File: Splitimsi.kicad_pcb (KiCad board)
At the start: 2 copper layers, 117.1 x 99.1 mm, 34 parts, among them SW1 MX_RGB, SW10 MX_RGB, SW11 MX_RGB, SW12 MX_RGB, SW13 MX_RGB, SW14 MX_RGB, SW15 MX_RGB, SW16 RotaryEncoder_Switch, SW17 MX_RGB, SW18 MX_RGB, SW19 MX_RGB, SW2 MX_RGB, SW20 MX_RGB, SW21 MX_RGB, SW22 MX_RGB, SW23 MX_RGB, SW24 MX_RGB, SW25 MX_RGB, SW26 MX_RGB, SW27 MX_RGB, SW28 MX_RGB, SW3 MX_RGB, SW4 MX_RGB, SW5 MX_RGB, SW6 MX_RGB, SW7 MX_RGB, SW8 MX_RGB, SW9 MX_RGB, U1 ProMicro, U2 TRRS

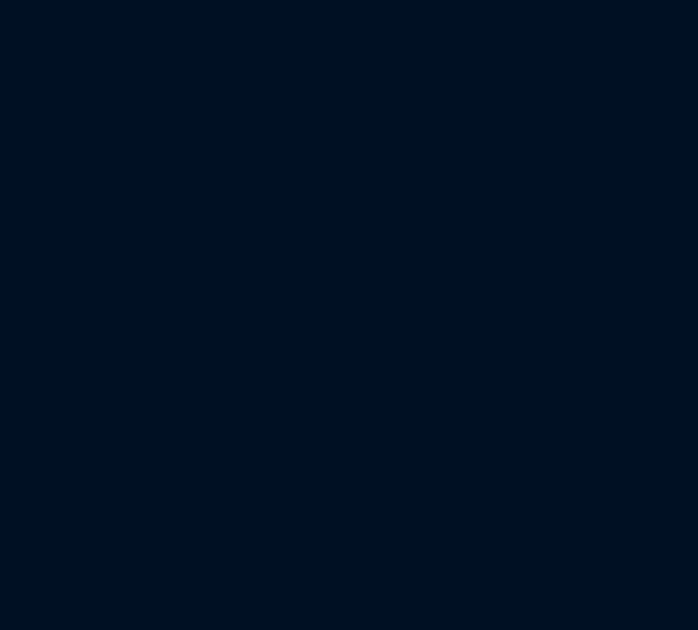
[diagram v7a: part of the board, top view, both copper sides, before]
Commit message: mounting holes added
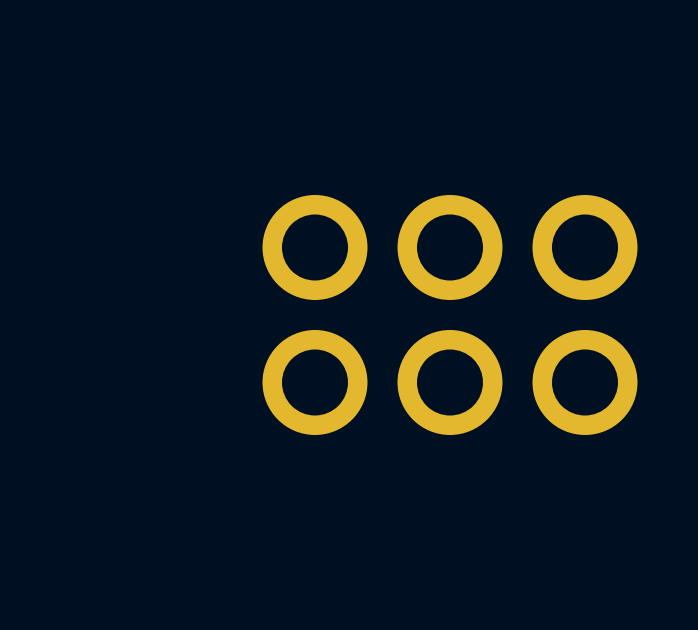
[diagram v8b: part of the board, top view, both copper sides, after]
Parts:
- added H1: Hole, aio3-misc:Generic-Mounthole, F.Cu at (167.0, 47.8)
- added H2: Hole, aio3-misc:Generic-Mounthole, F.Cu at (162.5, 47.8)
- added H3: Hole, aio3-misc:Generic-Mounthole, F.Cu at (158.0, 52.3)
- added H4: Hole, aio3-misc:Generic-Mounthole, F.Cu at (167.0, 52.3)
- added H5: Hole, aio3-misc:Generic-Mounthole, F.Cu at (158.0, 47.8)
- added H6: Hole, aio3-misc:Generic-Mounthole, F.Cu at (162.5, 52.3)
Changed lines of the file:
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@@
     )
+  )
+  (footprint "aio3-misc:Generic-Mounthole" (layer "F.Cu")
+    (at 157.992847 47.811959)
+    (property "Sheetfile" "Splitimsi.kicad_sch")
+    (property "Sheetname" "")
+    (attr exclude_from_pos_files)
+    (fp_text reference "H5" (at 0 2) (layer "Dwgs.User")
+      (effects (font (size 1 1) (thickness 0.15)))
+    )
+    (fp_text value "Hole" (at 0 -2) (layer "Dwgs.User")
+      (effects (font (size 1 1) (thickness 0.15)))
+    )
+    (pad "1" thru_hole circle locked (at 0 0) (size 3.5 3.5) (drill 2.2) (layers *.Cu *.Mask))
+  )
+  (footprint "aio3-misc:Generic-Mounthole" (layer "F.Cu")
+    (at 157.992847 52.311959)
+    (property "Sheetfile" "Splitimsi.kicad_sch")
+    (property "Sheetname" "")
+    (attr exclude_from_pos_files)
+    (fp_text reference "H3" (at 0 2) (layer "Dwgs.User")
+      (effects (font (size 1 1) (thickness 0.15)))
+    )
+    (fp_text value "Hole" (at 0 -2) (layer "Dwgs.User")
+      (effects (font (size 1 1) (thickness 0.15)))
+    )
+    (pad "1" thru_hole circle locked (at 0 0) (size 3.5 3.5) (drill 2.2) (layers *.Cu *.Mask))
+  )
+  (footprint "aio3-misc:Generic-Mounthole" (layer "F.Cu")
+    (at 162.492847 52.311959)
+    (property "Sheetfile" "Splitimsi.kicad_sch")
+    (property "Sheetname" "")
+    (attr exclude_from_pos_files)
+    (fp_text reference "H6" (at 0 2) (layer "Dwgs.User")
+      (effects (font (size 1 1) (thickness 0.15)))
+    )
+    (fp_text value "Hole" (at 0 -2) (layer "Dwgs.User")
+      (effects (font (size 1 1) (thickness 0.15)))
+    )
+    (pad "1" thru_hole circle locked (at 0 0) (size 3.5 3.5) (drill 2.2) (layers *.Cu *.Mask))
+  )
+  (footprint "aio3-misc:Generic-Mounthole" (layer "F.Cu")
+    (at 166.992847 47.811959)
+    (property "Sheetfile" "Splitimsi.kicad_sch")
+    (property "Sheetname" "")
+    (attr exclude_from_pos_files)
+    (fp_text reference "H1" (at 0 2) (layer "Dwgs.User")
+      (effects (font (size 1 1) (thickness 0.15)))
+    )
+    (fp_text value "Hole" (at 0 -2) (layer "Dwgs.User")
+      (effects (font (size 1 1) (thickness 0.15)))
+    )
+    (pad "1" thru_hole circle locked (at 0 0) (size 3.5 3.5) (drill 2.2) (layers *.Cu *.Mask))
   )
   (footprint "KeyboardCustomFPs:Kailh_HS_MX_LED" (layer "F.Cu")
@@
       (rotate (xyz 180 0 0))
     )
+  )
+  (footprint "aio3-misc:Generic-Mounthole" (layer "F.Cu")
+    (at 166.992847 52.311959)
+    (property "Sheetfile" "Splitimsi.kicad_sch")
+    (property "Sheetname" "")
+    (attr exclude_from_pos_files)
+    (fp_text reference "H4" (at 0 2) (layer "Dwgs.User")
+      (effects (font (size 1 1) (thickness 0.15)))
+    )
+    (fp_text value "Hole" (at 0 -2) (layer "Dwgs.User")
+      (effects (font (size 1 1) (thickness 0.15)))
+    )
+    (pad "1" thru_hole circle locked (at 0 0) (size 3.5 3.5) (drill 2.2) (layers *.Cu *.Mask))
   )
   (footprint "KeyboardCustomFPs:Kailh_HS_MX_LED" (layer "F.Cu")
@@
     )
   )
+  (footprint "aio3-misc:Generic-Mounthole" (layer "F.Cu")
+    (at 162.492847 47.811959)
+    (property "Sheetfile" "Splitimsi.kicad_sch")
+    (property "Sheetname" "")
+    (attr exclude_from_pos_files)
+    (fp_text reference "H2" (at 0 2) (layer "Dwgs.User")
+      (effects (font (size 1 1) (thickness 0.15)))
+    )
+    (fp_text value "Hole" (at 0 -2) (layer "Dwgs.User")
+      (effects (font (size 1 1) (thickness 0.15)))
+    )
+    (pad "1" thru_hole circle locked (at 0 0) (size 3.5 3.5) (drill 2.2) (layers *.Cu *.Mask))
+  )
   (footprint "KeyboardCustomFPs:Kailh_HS_MX_LED" (layer "F.Cu")
